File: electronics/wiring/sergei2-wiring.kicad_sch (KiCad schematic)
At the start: 35 parts, among them J1 6i25 port 1, J2 6i25 port 2, M1 UGRMEM, M101 Enclosure Fan, M102 Coolant Pump, M2 UGRMEM, M3 57BLF02, M4 Spindle, SW1 ESTOP, SW2 Mode switch, SW3 Run, SW4 Door closed, SW5 Pause, SW7 50°C NO, U1 Power_control_PCB, U3 BrakeShunt

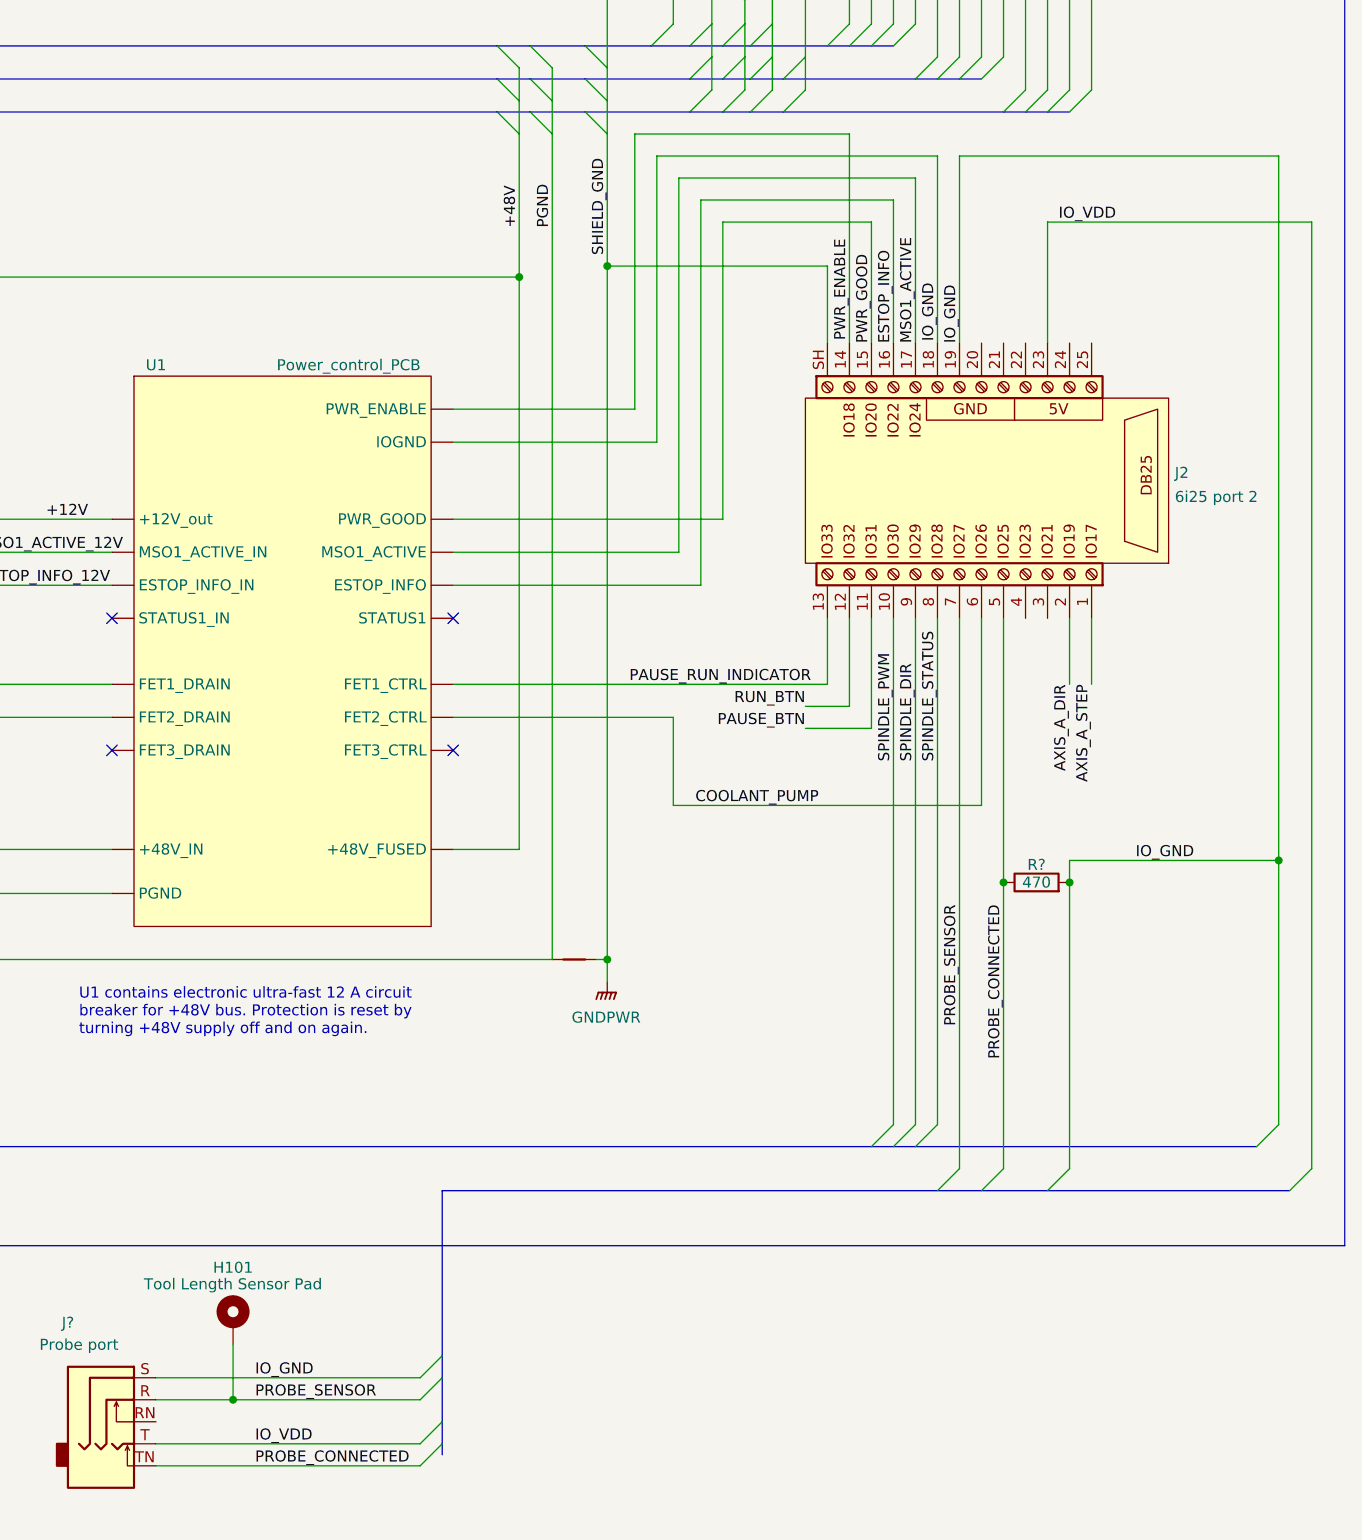
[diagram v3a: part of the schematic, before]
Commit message: Update wiring diagram
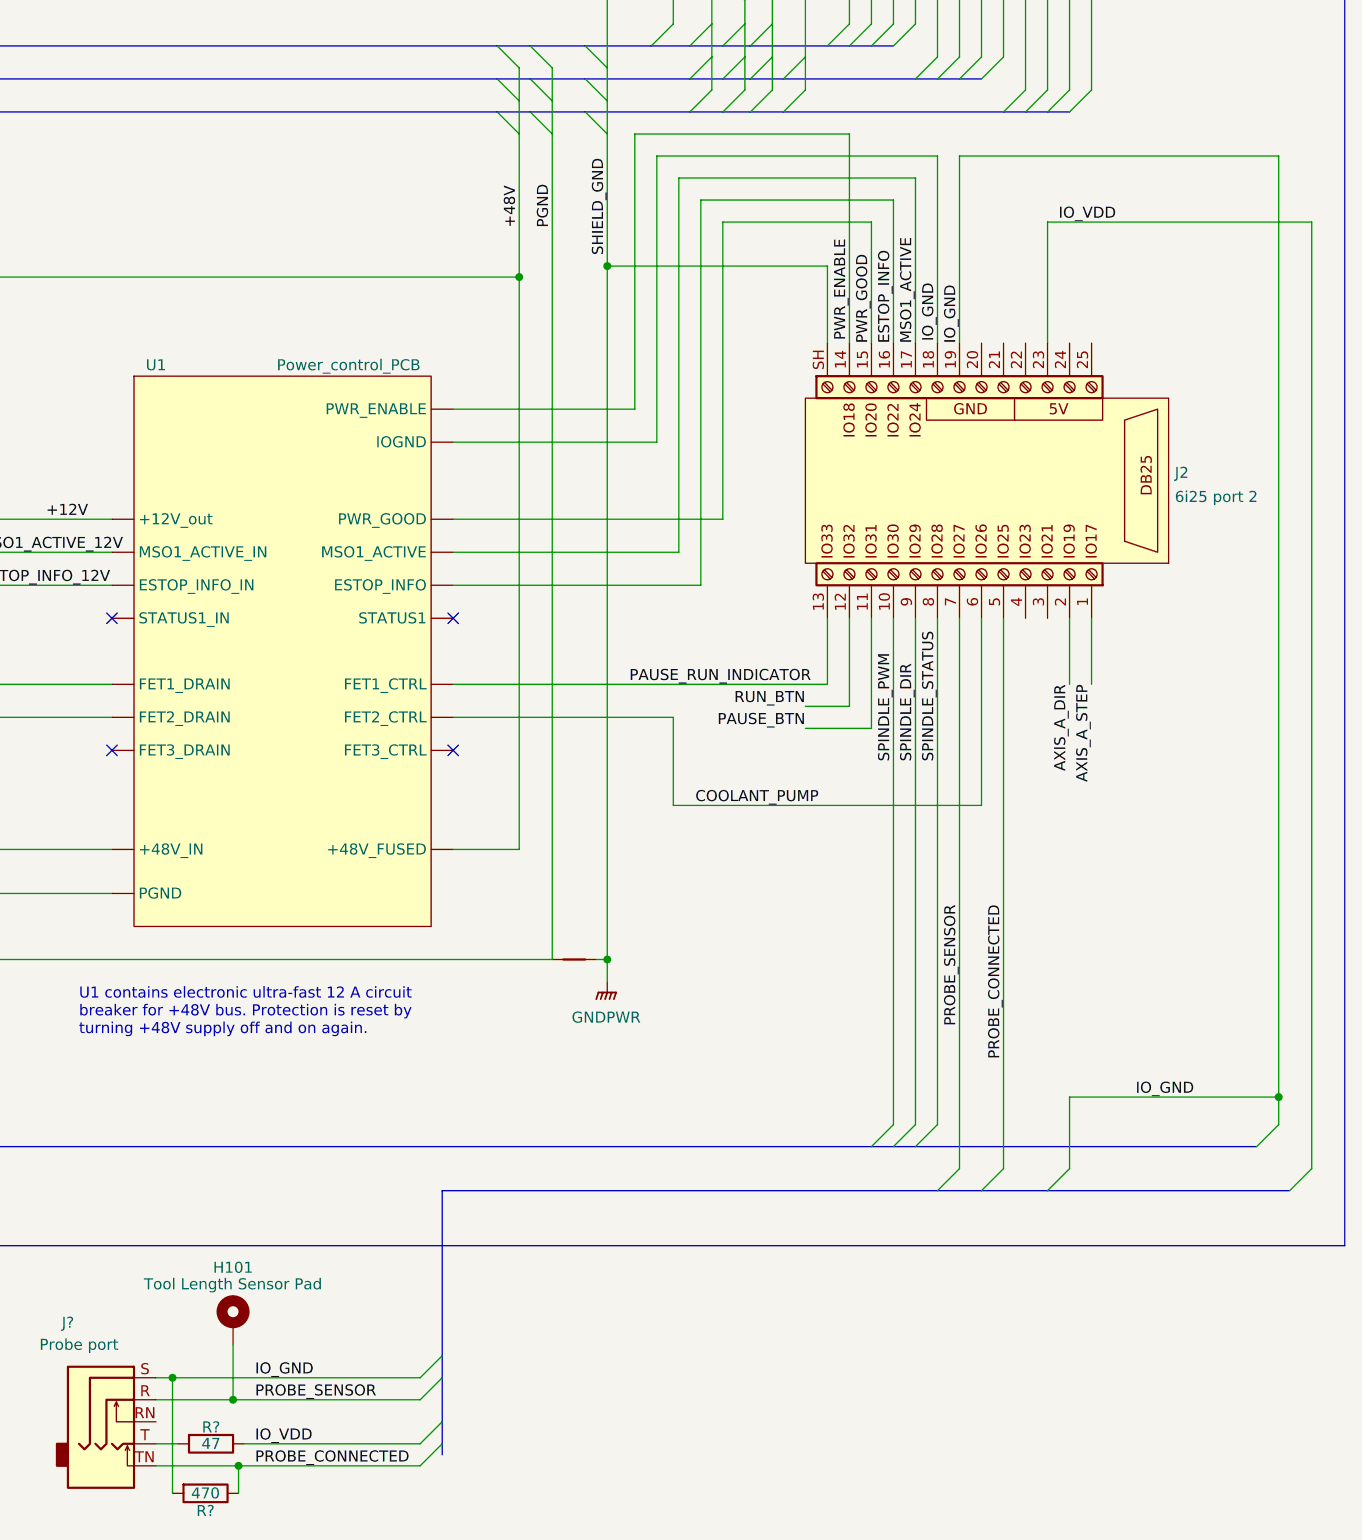
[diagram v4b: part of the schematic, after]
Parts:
- added R?: 47, symbol Device:R
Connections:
- net IO_VDD: now also R?.1; no longer J?.T
- new net: J?.T, R?.2
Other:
- moved on the sheet: R?
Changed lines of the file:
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@@
   (junction (at 232.41 201.93) (diameter 0) (color 0 0 0 0)
   )
-  (junction (at 364.49 200.66) (diameter 0) (color 0 0 0 0)
-  )
   (junction (at 359.41 38.1) (diameter 0) (color 0 0 0 0)
   )
@@
   (junction (at 196.215 266.7) (diameter 0) (color 0 0 0 0)
   )
+  (junction (at 260.985 257.81) (diameter 0) (color 204 102 0 1)
+  )
   (junction (at 83.82 149.86) (diameter 0) (color 0 0 0 0)
   )
-  (junction (at 388.62 198.12) (diameter 0) (color 0 0 0 0)
-  )
   (junction (at 349.25 40.64) (diameter 0) (color 0 0 0 0)
   )
@@
   (junction (at 327.025 38.1) (diameter 0) (color 0 0 0 0)
   )
-  (junction (at 356.87 200.66) (diameter 0) (color 0 0 0 0)
-  )
   (junction (at 149.86 237.49) (diameter 0) (color 0 0 0 0)
   )
@@
   (junction (at 311.15 209.55) (diameter 0) (color 0 0 0 0)
   )
+  (junction (at 388.62 225.425) (diameter 0) (color 0 0 0 0)
+  )
   (junction (at 300.99 130.81) (diameter 0) (color 0 0 0 0)
   )
@@
   )
   (junction (at 180.34 82.55) (diameter 0) (color 0 0 0 0)
+  )
+  (junction (at 268.605 267.97) (diameter 0) (color 0 0 0 0)
   )
   (junction (at 116.84 198.12) (diameter 0) (color 0 0 0 0)
@@
   )
   (bus_entry (at 289.56 257.81) (size 2.54 -2.54)
-    (stroke (width 0) (type default) (color 194 194 194 1))
+    (stroke (width 0) (type default) (color 204 102 0 1))
   )
   (bus_entry (at 302.26 111.76) (size 2.54 2.54)
@@
   )
   (bus_entry (at 361.95 236.22) (size 2.54 -2.54)
-    (stroke (width 0) (type default) (color 194 194 194 1))
+    (stroke (width 0) (type default) (color 204 102 0 1))
   )
   (bus_entry (at 316.23 104.14) (size 2.54 -2.54)
@@
   )
   (bus_entry (at 389.89 236.22) (size 2.54 -2.54)
-    (stroke (width 0) (type default) (color 204 102 0 1))
+    (stroke (width 0) (type default) (color 194 194 194 1))
   )
   (bus_entry (at 356.87 111.76) (size 2.54 -2.54)
@@
   )
   (bus_entry (at 289.56 265.43) (size 2.54 -2.54)
-    (stroke (width 0) (type default) (color 204 102 0 1))
+    (stroke (width 0) (type default) (color 194 194 194 1))
   )
   (bus_entry (at 215.9 59.69) (size 2.54 2.54)
@@
     (stroke (width 0) (type default) (color 0 0 0 0))
   )
-  (wire (pts (xy 364.49 233.68) (xy 364.49 200.66))
-    (stroke (width 0) (type default) (color 194 194 194 1))
+  (wire (pts (xy 364.49 233.68) (xy 364.49 225.425))
+    (stroke (width 0) (type default) (color 204 102 0 1))
   )
   (wire (pts (xy 300.99 110.49) (xy 300.99 114.3))
@@
     (stroke (width 0) (type default) (color 0 0 0 0))
   )
-  (wire (pts (xy 356.87 200.66) (xy 356.87 233.68))
+  (wire (pts (xy 356.87 170.18) (xy 356.87 233.68))
     (stroke (width 0) (type default) (color 0 0 0 0))
   )
@@
     (stroke (width 0) (type default) (color 0 0 0 0))
   )
-  (wire (pts (xy 388.62 198.12) (xy 388.62 116.84))
-    (stroke (width 0) (type default) (color 0 0 0 0))
-  )
   (wire (pts (xy 200.66 130.81) (xy 200.66 134.62))
     (stroke (width 0) (type default) (color 0 0 0 0))
@@
   )
   (wire (pts (xy 137.16 189.23) (xy 137.16 198.12))
+    (stroke (width 0) (type default) (color 0 0 0 0))
+  )
+  (wire (pts (xy 259.08 265.43) (xy 261.62 265.43))
     (stroke (width 0) (type default) (color 0 0 0 0))
   )
@@
     (stroke (width 0.7) (type default) (color 204 102 0 1))
   )
+  (wire (pts (xy 268.605 267.97) (xy 289.56 267.97))
+    (stroke (width 0) (type default) (color 0 0 0 0))
+  )
   (wire (pts (xy 109.22 243.84) (xy 105.41 243.84))
     (stroke (width 0) (type default) (color 0 0 0 0))
@@
   )
   (wire (pts (xy 392.43 233.68) (xy 392.43 124.46))
-    (stroke (width 0) (type default) (color 0 0 0 0))
+    (stroke (width 0) (type default) (color 194 194 194 1))
   )
   (wire (pts (xy 124.46 67.31) (xy 107.95 67.31))
@@
     (stroke (width 0.4) (type default) (color 194 194 194 1))
   )
-  (wire (pts (xy 388.62 228.6) (xy 388.62 198.12))
+  (wire (pts (xy 388.62 228.6) (xy 388.62 225.425))
     (stroke (width 0) (type default) (color 0 0 0 0))
   )
@@
     (stroke (width 0) (type default) (color 0 0 0 0))
   )
+  (wire (pts (xy 388.62 116.84) (xy 388.62 225.425))
+    (stroke (width 0) (type default) (color 0 0 0 0))
+  )
   (wire (pts (xy 65.405 39.37) (xy 48.895 39.37))
     (stroke (width 0) (type default) (color 0 0 255 1))
@@
     (stroke (width 0) (type default) (color 0 0 0 0))
   )
+  (wire (pts (xy 260.985 257.81) (xy 260.985 271.145))
+    (stroke (width 0) (type default) (color 204 102 0 1))
+  )
   (wire (pts (xy 180.975 39.37) (xy 164.465 39.37))
     (stroke (width 0) (type default) (color 0 0 255 1))
@@
     (stroke (width 0) (type default) (color 0 0 0 0))
   )
-  (wire (pts (xy 259.08 257.81) (xy 289.56 257.81))
-    (stroke (width 0) (type default) (color 194 194 194 1))
+  (wire (pts (xy 259.08 257.81) (xy 260.985 257.81))
+    (stroke (width 0) (type default) (color 204 102 0 1))
   )
   (bus (pts (xy 218.44 231.14) (xy 341.63 231.14))
@@
     (stroke (width 0) (type default) (color 0 0 0 0))
   )
+  (wire (pts (xy 268.605 267.97) (xy 268.605 271.145))
+    (stroke (width 0) (type default) (color 0 0 0 0))
+  )
   (bus (pts (xy 127 57.15) (xy 127 59.69))
     (stroke (width 0) (type default) (color 0 0 0 0))
@@
     (stroke (width 0) (type default) (color 0 0 0 0))
   )
+  (wire (pts (xy 260.985 257.81) (xy 289.56 257.81))
+    (stroke (width 0) (type default) (color 204 102 0 1))
+  )
   (wire (pts (xy 318.77 191.77) (xy 354.33 191.77))
     (stroke (width 0) (type default) (color 0 0 0 0))
@@
     (stroke (width 0) (type default) (color 0 0 0 0))
   )
-  (wire (pts (xy 364.49 198.12) (xy 388.62 198.12))
+  (wire (pts (xy 364.49 225.425) (xy 388.62 225.425))
     (stroke (width 0) (type default) (color 0 0 0 0))
   )
@@
     (stroke (width 0) (type default) (color 0 0 0 0))
   )
-  (wire (pts (xy 259.08 267.97) (xy 289.56 267.97))
+  (wire (pts (xy 259.08 267.97) (xy 268.605 267.97))
     (stroke (width 0) (type default) (color 0 0 0 0))
   )
@@
     (stroke (width 0) (type default) (color 0 0 0 0))
   )
-  (wire (pts (xy 259.08 265.43) (xy 289.56 265.43))
-    (stroke (width 0) (type default) (color 204 102 0 1))
-  )
   (wire (pts (xy 232.41 270.51) (xy 232.41 209.55))
     (stroke (width 0) (type default) (color 0 0 0 0))
@@
     (stroke (width 0) (type default) (color 0 0 0 0))
   )
+  (wire (pts (xy 269.24 265.43) (xy 289.56 265.43))
+    (stroke (width 0) (type default) (color 194 194 194 1))
+  )
   (wire (pts (xy 149.86 90.17) (xy 149.86 85.09))
     (stroke (width 0) (type default) (color 0 0 0 0))
@@
     (stroke (width 0) (type default) (color 204 102 0 1))
   )
-  (wire (pts (xy 364.49 200.66) (xy 364.49 198.12))
-    (stroke (width 0) (type default) (color 0 0 0 0))
-  )
   (wire (pts (xy 177.8 96.52) (xy 215.9 96.52))
     (stroke (width 0) (type default) (color 0 0 0 0))
@@
   )
   (bus (pts (xy 316.23 104.14) (xy 320.675 104.14))
-    (stroke (width 0) (type default) (color 0 0 0 0))
-  )
-  (wire (pts (xy 356.87 170.18) (xy 356.87 200.66))
     (stroke (width 0) (type default) (color 0 0 0 0))
   )
@@
     (effects (font (size 1.27 1.27)) (justify right bottom))
   )
-  (label "IO_GND" (at 372.11 198.12 0)
+  (label "IO_GND" (at 372.11 225.425 0)
     (effects (font (size 1.27 1.27)) (justify left bottom))
   )
@@
     (pin "2")
   )
+  (symbol (lib_id "Device:R") (at 265.43 265.43 270) (unit 1)
+    (in_bom yes) (on_board yes)
+    (property "Reference" "R?" (id 0) (at 265.43 263.525 90))
+    (property "Value" "47" (id 1) (at 265.43 265.43 90))
+    (property "Footprint" "" (id 2) (at 265.43 263.652 90)
+      (effects (font (size 1.27 1.27)) hide)
+    )
+    (property "Datasheet" "~" (id 3) (at 265.43 265.43 0)
+      (effects (font (size 1.27 1.27)) hide)
+    )
+    (pin "1")
+    (pin "2")
+  )
   (symbol (lib_id "Converter_ACDC:VTX-214-015-112") (at 171.45 234.95 0) (unit 1)
     (in_bom yes) (on_board yes)
@@
     (pin "NO1B")
   )
-  (symbol (lib_id "Device:R") (at 360.68 200.66 90) (unit 1)
+  (symbol (lib_id "Device:R") (at 264.795 271.145 270) (unit 1)
     (in_bom yes) (on_board yes)
-    (property "Reference" "R?" (id 0) (at 360.68 198.628 90))
-    (property "Value" "470" (id 1) (at 360.68 200.66 90))
-    (property "Footprint" "" (id 2) (at 360.68 202.438 90)
-      (effects (font (size 1.27 1.27)) hide)
-    )
-    (property "Datasheet" "~" (id 3) (at 360.68 200.66 0)
+    (property "Reference" "R?" (id 0) (at 264.795 273.177 90))
+    (property "Value" "470" (id 1) (at 264.795 271.145 90))
+    (property "Footprint" "" (id 2) (at 264.795 269.367 90)
+      (effects (font (size 1.27 1.27)) hide)
+    )
+    (property "Datasheet" "~" (id 3) (at 264.795 271.145 0)
       (effects (font (size 1.27 1.27)) hide)
     )
@@
       (reference "R2") (unit 1) (value "10R") (footprint "")
     )
+    (path "/717d6288-9cd9-46a8-a063-2f515d086805"
+      (reference "R?") (unit 1) (value "47") (footprint "")
+    )
     (path "/c06182d7-d232-4b51-a000-23f0ae2babaa"
